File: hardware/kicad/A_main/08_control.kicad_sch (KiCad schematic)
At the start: 26 parts, among them J60 GPS modul, J61 SMA 10MHz ref, J62 DAC modul, J63 C kartina, J64 UART 3.3V, J65 C kartina #2, J66 D kartina, U10 LFE5U-25F-7BG256I, U62 TLV3501AIDBVR

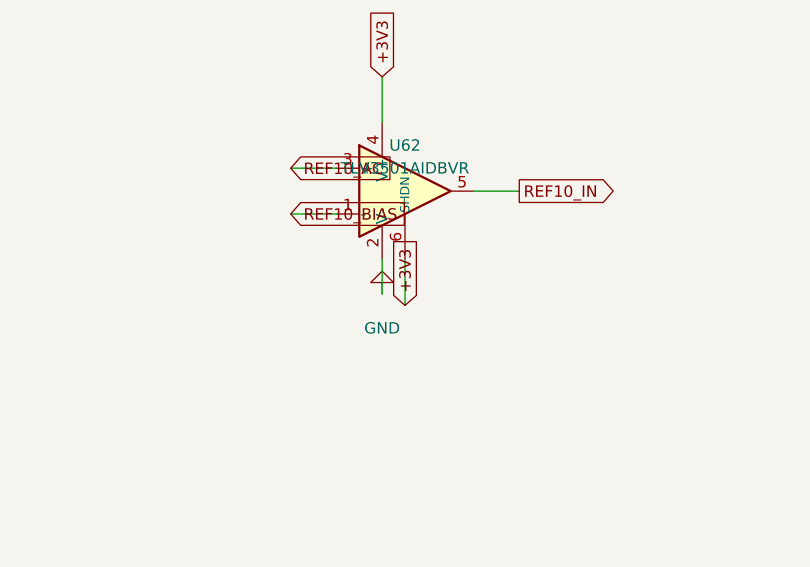
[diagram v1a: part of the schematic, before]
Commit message: Remove the pads that have no copper from the DSN export
The router reported the same 220 clearance violations in each pass.
At the same time the number of unrouted connections decreased. The
violations were thus in the input and not in the routing.

The -1EP footprints of KiCad put four paste apertures on the exposed
pad. These apertures stop full paste coverage and they have no copper
layer. The DSN export put them on the top copper layer. The image of
U51 in the DSN had 21 pins: 17 correct pins and four unconnected
copper islands in the exposed pad. These islands are always in
conflict with the pad and they close the area below it.

The export now removes a pad that has no copper layer. The image of
U51 has 17 pins. The violations on board D decreased from 220 to 152.
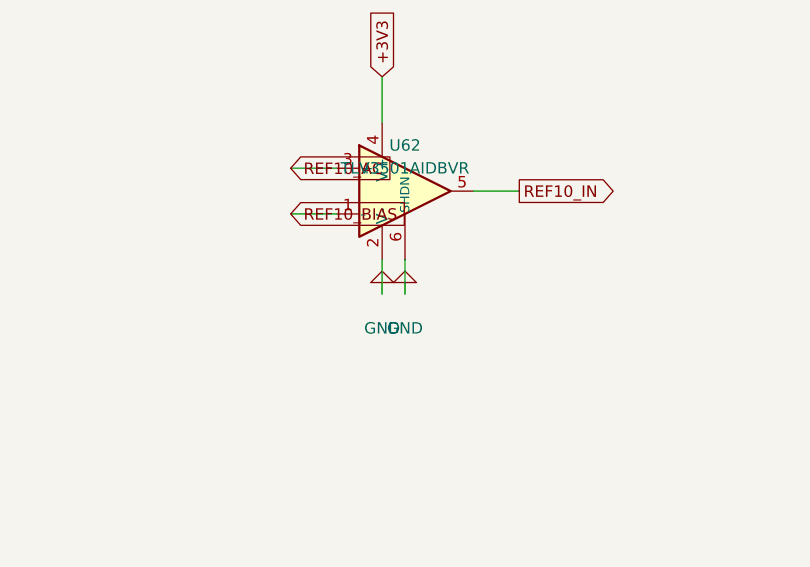
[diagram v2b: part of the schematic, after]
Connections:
- net +3V3: no longer U62.6 (SHDN)
- net GND: now also U62.6 (SHDN)

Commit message: Correct the clearance test for the pre-routed traces
The clearance test used a circle for each pad. The radius was
max(width, height)/2. The corner of a rectangle is at
hypot(width, height)/2 from the center. The test thus made the pad
smaller than it is. On the 2.5 x 4.5 mm gate pad of a TO-247 the
difference is 2.250 mm against 2.574 mm.

The DRN_A trace was on the gate pad of Q10 with an overlap of 35 um.
This is a short circuit between the 50 V drain rail and the gate of a
100 W device. The search that finds the tee offset accepted this
route. The overlap is at a corner and 35 um wide. You cannot see it
on a plot.

The test now uses the real shape of the pad and the collision test of
pcbnew. It also uses the 300 um clearance and not only an overlap. A
trace that is 50 um from a pad is also not possible to manufacture.

Board D was built again. No trace is below 300 um and the smallest
gap is 0.537 mm. Boards A and C were correct.
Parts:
- removed C900, C901, C902: 100nF, Capacitor_SMD:C_0603_1608Metric, symbol Device:C
- removed D60: yesil, LED_SMD:LED_0805_2012Metric, symbol Device:LED
- removed D61: mavi, LED_SMD:LED_0805_2012Metric, symbol Device:LED
- removed D62: kirmizi, LED_SMD:LED_0805_2012Metric, symbol Device:LED
- removed D63: sari, LED_SMD:LED_0805_2012Metric, symbol Device:LED
- removed J60: GPS modul, Connector_PinHeader_2.54mm:PinHeader_1x06_P2.54mm_Vertical, symbol Connector_Generic:Conn_01x06
- removed J61: SMA 10MHz ref, Connector_Coaxial:SMA_Amphenol_132289_EdgeMount, symbol Connector:Conn_Coaxial
- removed J62: DAC modul, Connector_PinHeader_2.54mm:PinHeader_1x06_P2.54mm_Vertical, symbol Connector_Generic:Conn_01x06
- removed J63: C kartina, Connector_PinHeader_2.54mm:PinHeader_2x10_P2.54mm_Vertical, symbol Connector_Generic:Conn_02x10_Odd_Even
- removed J64: UART 3.3V, Connector_PinHeader_2.54mm:PinHeader_1x04_P2.54mm_Vertical, symbol Connector_Generic:Conn_01x04
- removed J65: C kartina #2, Connector_PinHeader_2.54mm:PinHeader_1x06_P2.54mm_Vertical, symbol Connector_Generic:Conn_01x06
- removed J66: D kartina, Connector_PinHeader_2.54mm:PinHeader_2x10_P2.54mm_Vertical, symbol Connector_Generic:Conn_02x10_Odd_Even
- removed R60, R61, R62, R63: 1k, Resistor_SMD:R_0603_1608Metric, symbol Device:R
- removed R801: 0R, Resistor_SMD:R_0603_1608Metric, symbol Device:R
- removed R900: 50R 1%, Resistor_SMD:R_0603_1608Metric, symbol Device:R
- removed R901, R902, R903, R904: 10k, Resistor_SMD:R_0603_1608Metric, symbol Device:R
- removed U10: LFE5U-25F-7BG256I, Package_BGA:BGA-256_14.0x14.0mm_Layout16x16_P0.8mm_Ball0.45mm_Pad0.32mm_NSMD, symbol dogrudan-sdr:ECP5-BGA256
- removed U62: TLV3501AIDBVR, Package_TO_SOT_SMD:SOT-23-6, symbol Comparator:TLV3501AIDBV
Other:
- note added: "Kontrol PE4312 x2, GPS, VCXO DAC, roleler, banka 0/1 Baglantilar: ../NETLIST.md"
- note removed: "3.3 V TTL, CP2102/FT232 tarzi ucuz donusturucu takilir. Bringup'ta FPGA icindeki yazilim buradan konusuyor; JTAG'den once calisan tek gozlem yolu."
- note removed: "ANOT +3V3'te, FPGA KATODU CEKIYOR (aktif dusuk). Boyle secildi cunku ECP5'in IO'su akim CEKMEKTE (sink) akim VERMEKTEN (source) daha guclu: 3.3V bankada 8 mA sink, source tarafinda gerilim dusuyor ve LED sonuk kaliyor. 1k ile 3.3V'ta ~1.6 mA — 0805 LED icin fazlasiyla gorunur, dort LED toplam 6.4 mA. Parlaklik isterse 470R'a inilir. STATUS gateware kalkti / PLL kilitli RX alis zinciri veri uretiy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"
- note removed: "BANKA 0: 24 I/O, TAMAMI DOLU. SDRAM tasmasi 7 (A9-A12, BA0/1, UDQM) ADC SPI+SYNC 5 SDIO, SCLK, 2x nCSB, SYNC ortak seri yol 2 ATT_DATA, ATT_CLK secme hatlari 7 ATT1..4_LE, PA_ATT_LE, BIAS_CS1/CS2 PA'nin ADC'si 1 PA_ADC_CS role yazmaci 3 SER/SRCLK/RCLK ADC PDWN ve DAC SLEEP hatlari KALDIRILDI. Bu alet ya acik ya kapali; guc-dusurme kontrolu hic kullanilmiyor. Dordu de kendi sayfalarinda GND'ye bag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"
- note removed: "BANKA 1: 32/32, MARJ YOK. DAC-2 interleaved 17 · GPS 3 · VCXO DAC 3 · hata ayiklama UART 2 harici 10 MHz 1 · role RCLK 1 · T/R 4 · PA_INHIBIT 1 PA_INHIBIT yedek pini aldi. Donanim kesme hatti: FPGA sifirlaninca ya da beslemesizken D kartinda 100k asagi cekiyor ve surucu beslemesiz kaliyor. Bu hattin seri yola girmesi kabul edilemez — guvenlik dogrudan olmali. Durum LED'leri buraya sigmadi — 07_fp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"
- note removed: "D KARTINA (PA)"
- note removed: "DAC parcasi HENUZ SECILMEDI — 16 bit, dusuk gurultulu, SPI. Vc gurultusu dogrudan faz gurultusune donusuyor, o yuzden beslemesi +3V3_CLK (VCXO'nun kendi LDO'su). Baslik olarak cizildi; parca secilince yerine konacak."
- note removed: "DURUM LED'LERI"
- note removed: "FPGA BANKA 0 — kontrol ve SDRAM tasmasi"
- note removed: "FPGA BANKA 1 — GPSDO, DAC-2, durum"
- note removed: "GPS / GPSDO ARAYUZU"
- note removed: "HARICI 10 MHz — SMA, 50R sonlandirma, AC kuplaj, KOMPARATOR. Iki 10k bolucu orta gerilim (1.65 V) uretiyor: sinyal bacagi o gerilim etrafinda salınıyor, referans bacagi ayni gerilimde sabit (100nF ile susturulmus). Komparator birkac yuz mV'luk sinusu tam salinimli kare dalgaya ceviriyor. TLV3501AIDBVR, LCSC C193413, $1.57, 1850 stok, SOT-23-6. 4.5 ns gecikme, rail-to-rail giris, tek 3.3 V besleme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"
- note removed: "HATA AYIKLAMA UART"
- note removed: "HER SINYALIN YANINDA TOPRAK. 2.54 mm baslikta bitisik toprak donus yolunu kisaltiyor; role hatlari 12 V anahtarliyor ve kenarlari sert, yanindaki RF'e kuplaj yapmasin. ATT2 hatlari ve +12 V ikinci baslikta (yerlesimde eklenecek). RF kart arasi koaks kuyrukla — baslikla DEGIL. Toprak GND_HDR uzerinden 0R ile ana topraga: tek nokta, gerekirse ayrilabiliyor."
- note removed: "KART ARASI — A <-> C, NETLIST.md §8"
- note removed: "PA'nin istedigi 13 sinyal 5 YENI HATLA karsilandi: ATT_DATA / ATT_CLK -> C kartiyla ORTAK, yeni hat yok ADC_SDIO -> ortak MISO, AD9251'in hatti role zinciri -> D'ye C KARTINDAN gidiyor, A'dan degil PA_ATT_LE, BIAS_CS1, BIAS_CS2, PA_ADC_CS, PA_INHIBIT -> yeni FLANGE_T, FWD_LOG, REV_LOG analog olcumleri A kartina GELMIYOR: D kartinda bir MCP3208 (8 kanal 12 bit SPI ADC) var, ayni seri yolu paylasiy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"
- note removed: "PE4312 x2, 0-31.5 dB. Her birine uc hat: Data / Clock / LE. Seri mod (P/S = HIGH). Paralel modda alti adres bacagini surmek gerekirdi, iki cip icin 12 pin ederdi. ACILIS DURUMU C KARTINDA COZULUYOR: seri modda bile acilistaki zayiflatma C0.5..C16 bacaklarindaki seviyeye gore belirleniyor (veri sayfasi s.6). Altisi da 10k ile yukari -> 31.5 dB, yani acilista alici en sagir halinde. FPGA flash'tan 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"
- note removed: "VCXO Vc — SPI DAC"
- note removed: "ZAYIFLATICI KONTROLU — cipler C KARTINDA"

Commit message: Correct the schematic faults that ERC cannot find
An agent examined the three schematics against the datasheets. ERC
reported zero violations before and after this work. None of these
faults are visible to ERC.

The comparator for the external 10 MHz reference was in shutdown. The
SHDN pin of the TLV3501 went to +3V3. Sixteen DRV8833 devices had VCP
and VINT unconnected. Without the charge pump none of the 28 filter
relays can latch. Seven regulators had no decoupling capacitor within
18 mm to 94 mm. On board D the nearest +12V capacitor to an LM358 was
227 mm away on a 275 mm board.

The PE4312 devices had no series 10k resistor on pin 3. The datasheet
makes this necessary for the attenuation accuracy. Their exposed pad
was 2.6 mm against 2.15 mm. The BOM did not give the load capacitance
of the crystal. This work added 60 parts and changed 4 footprints.

The worst fault was in the tool chain. lib/gen_symbols.py still made
the old pin numbers. The five corrections went into the symbol
library by hand and not into its generator. A new library would have
removed all of them.

The thermal vias are now a decision from the measured clearance and
the dissipation. This work removed them from the PE4312, the RTL8211F
and the ADCLK846. They stay on the DRV8833 and on the LM5164, which
is a 1 W buck converter.

Two checks are new. sema_denetim compares the pin names with the
nets. netlist_denetim locks 22 pin-to-net expectations from the
datasheets and does not need a board.

The boards were built again with these corrections. The chain now
adds the test points: 10 on board A, 7 on board C and 15 on board D.
Each board has 3 fiducials. Every pad has a net.
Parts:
- added C900, C901, C902: 100nF, Capacitor_SMD:C_0603_1608Metric, symbol Device:C
- added D60: yesil, LED_SMD:LED_0805_2012Metric, symbol Device:LED
- added D61: mavi, LED_SMD:LED_0805_2012Metric, symbol Device:LED
- added D62: kirmizi, LED_SMD:LED_0805_2012Metric, symbol Device:LED
- added D63: sari, LED_SMD:LED_0805_2012Metric, symbol Device:LED
- added J60: GPS modul, Connector_PinHeader_2.54mm:PinHeader_1x06_P2.54mm_Vertical, symbol Connector_Generic:Conn_01x06
- added J61: SMA 10MHz ref, Connector_Coaxial:SMA_Amphenol_132289_EdgeMount, symbol Connector:Conn_Coaxial
- added J62: DAC modul, Connector_PinHeader_2.54mm:PinHeader_1x06_P2.54mm_Vertical, symbol Connector_Generic:Conn_01x06
- added J63: C kartina, Connector_PinHeader_2.54mm:PinHeader_2x10_P2.54mm_Vertical, symbol Connector_Generic:Conn_02x10_Odd_Even
- added J64: UART 3.3V, Connector_PinHeader_2.54mm:PinHeader_1x04_P2.54mm_Vertical, symbol Connector_Generic:Conn_01x04
- added J65: C kartina #2, Connector_PinHeader_2.54mm:PinHeader_1x06_P2.54mm_Vertical, symbol Connector_Generic:Conn_01x06
- added J66: D kartina, Connector_PinHeader_2.54mm:PinHeader_2x10_P2.54mm_Vertical, symbol Connector_Generic:Conn_02x10_Odd_Even
- added R60, R61, R62, R63: 1k, Resistor_SMD:R_0603_1608Metric, symbol Device:R
- added R801: 0R, Resistor_SMD:R_0603_1608Metric, symbol Device:R
- added R900: 50R 1%, Resistor_SMD:R_0603_1608Metric, symbol Device:R
- added R901, R902, R903, R904: 10k, Resistor_SMD:R_0603_1608Metric, symbol Device:R
- added U10: LFE5U-25F-7BG256I, Package_BGA:BGA-256_14.0x14.0mm_Layout16x16_P0.8mm_Ball0.45mm_Pad0.32mm_NSMD, symbol dogrudan-sdr:ECP5-BGA256
- added U62: TLV3501AIDBVR, Package_TO_SOT_SMD:SOT-23-6, symbol Comparator:TLV3501AIDBV
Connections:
- new net +3V3: C902.1, D60.2 (A), D61.2 (A), D62.2 (A), D63.2 (A), J60.1 (Pin_1), J63.1 (Pin_1), J64.1 (Pin_1), J65.5 (Pin_5), J66.1 (Pin_1), R901.1, R903.1, U10.F10 (VCCIO1_1), U10.F11 (VCCIO1_2), U10.F6 (VCCIO0_1), U10.F7 (VCCIO0_2), U62.4 (V+)
- new net +3V3_CLK: J62.1 (Pin_1)
- new net ADC1_nCSB: U10.B5 (PT15B)
- new net ADC2_nCSB: U10.B6 (PT22B)
- new net ADC_SCLK: U10.B4 (PT11B)
- new net ADC_SDIO: J66.17 (Pin_17), U10.B3 (PT4B)
- new net ADC_SYNC: U10.B7 (PT27B)
- new net ATT1_LE: J63.19 (Pin_19), U10.C6 (PT22A)
- new net ATT2_LE: J65.1 (Pin_1), U10.C7 (PT27A)
- new net ATT3_LE: J65.2 (Pin_2), U10.D4 (PT9B)
- new net ATT4_LE: J65.3 (Pin_3), U10.D5 (PT13B)
- new net ATT_CLK: J63.18 (Pin_18), J66.5 (Pin_5), U10.C5 (PT15A)
- new net ATT_DATA: J63.17 (Pin_17), J66.3 (Pin_3), U10.C4 (PT11A)
- new net BIAS_CS1: J66.9 (Pin_9), U10.D7 (PT24B)
- new net BIAS_CS2: J66.11 (Pin_11), U10.E4 (PT9A)
- new net DAC2_D0: U10.A9 (PT42A)
- new net DAC2_D1: U10.B9 (PT38A)
- new net DAC2_D10: U10.B13 (PT60A)
- new net DAC2_D11: U10.A14 (PT65B)
- new net DAC2_D12: U10.B14 (PT67A)
- new net DAC2_D13: U10.A15 (PT67B)
- new net DAC2_D2: U10.D9 (PT40A)
- new net DAC2_D3: U10.A10 (PT42B)
- new net DAC2_D4: U10.B10 (PT44A)
- new net DAC2_D5: U10.A11 (PT53A)
- new net DAC2_D6: U10.B11 (PT49A)
- new net DAC2_D7: U10.A12 (PT53B)
- new net DAC2_D8: U10.B12 (PT56A)
- new net DAC2_D9: U10.A13 (PT65A)
- new net DAC2_IQRESET: U10.C10 (PT44B)
- new net DAC2_IQSEL: U10.C11 (PT49B)
- new net DAC2_IQWRT: U10.B8 (PT35B)
- new net DBG_RX: J64.2 (Pin_2), U10.D12 (PT58A)
- new net DBG_TX: J64.3 (Pin_3), U10.D13 (PT62A)
- new net GND: C901.2, C902.2, J60.5 (Pin_5), J60.6 (Pin_6), J61.2 (Ext), J62.6 (Pin_6), J64.4 (Pin_4), J65.6 (Pin_6), R801.2, R900.2, R902.2, R904.2, U62.2 (V-), U62.6 (SHDN)
- new net GND_HDR: J63.10 (Pin_10), J63.12 (Pin_12), J63.14 (Pin_14), J63.16 (Pin_16), J63.2 (Pin_2), J63.4 (Pin_4), J63.6 (Pin_6), J63.8 (Pin_8), J66.10 (Pin_10), J66.12 (Pin_12), J66.14 (Pin_14), J66.16 (Pin_16), J66.18 (Pin_18), J66.19 (Pin_19), J66.2 (Pin_2), J66.20 (Pin_20), J66.4 (Pin_4), J66.6 (Pin_6), J66.8 (Pin_8), R801.1
- new net GPS_1PPS: J60.4 (Pin_4), U10.C12 (PT56B)
- new net GPS_RX: J60.2 (Pin_2), U10.C13 (PT60B)
- new net GPS_TX: J60.3 (Pin_3), U10.C8 (PT35A)
- new net LED_DATA: R63.2
- new net LED_DATA_K: D63.1 (K), R63.1
- new net LED_RX: R61.2
- new net LED_RX_K: D61.1 (K), R61.1
- new net LED_STATUS: R60.2
- new net LED_STATUS_K: D60.1 (K), R60.1
- new net LED_TX: R62.2
- new net LED_TX_K: D62.1 (K), R62.1
- new net PA_ADC_CS: J66.13 (Pin_13), U10.E5 (PT13A)
- new net PA_ATT_LE: J66.7 (Pin_7), U10.D6 (PT20B)
- new net PA_INHIBIT: J66.15 (Pin_15), U10.E9 (PT40B)
- new net REF10_AC: C900.2, R901.2, R902.1, U62.3 (+)
- new net REF10_BIAS: C901.1, R903.2, R904.1, U62.1 (-)
- new net REF10_IN: U10.D8 (PT33B), U62.5
- new net REF10_RAW: C900.1, J61.1 (In), R900.1
- new net RLY_RCLK: J63.7 (Pin_7), U10.E10 (PT47B)
- new net RLY_SER: J63.3 (Pin_3), U10.E6 (PT20A)
- new net RLY_SRCLK: J63.5 (Pin_5), U10.E7 (PT24A)
- new net SD_A10: U10.A2 (PT4A)
- new net SD_A11: U10.A6 (PT18B)
- new net SD_A12: U10.A7 (PT29A)
- new net SD_A9: U10.A5 (PT18A)
- new net SD_BA0: U10.A3 (PT6A)
- new net SD_BA1: U10.A4 (PT6B)
- new net SD_UDQM: U10.A8 (PT29B)
- new net TR1: J63.9 (Pin_9), U10.E11 (PT51B)
- new net TR2: J63.11 (Pin_11), U10.E12 (PT58B)
- new net TR3: J63.13 (Pin_13), U10.E13 (PT62B)
- new net TR4: J63.15 (Pin_15), U10.E8 (PT33A)
- new net VCXO_CLK: J62.3 (Pin_3), U10.D10 (PT47A)
- new net VCXO_CS: J62.2 (Pin_2), U10.C9 (PT38B)
- new net VCXO_DIN: J62.4 (Pin_4), U10.D11 (PT51A)
- new net VCXO_VC: J62.5 (Pin_5)
- new net VIN_PROT: J63.20 (Pin_20), J65.4 (Pin_4)
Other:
- note added: "3.3 V TTL, CP2102/FT232 tarzi ucuz donusturucu takilir. Bringup'ta FPGA icindeki yazilim buradan konusuyor; JTAG'den once calisan tek gozlem yolu."
- note added: "ANOT +3V3'te, FPGA KATODU CEKIYOR (aktif dusuk). Boyle secildi cunku ECP5'in IO'su akim CEKMEKTE (sink) akim VERMEKTEN (source) daha guclu: 3.3V bankada 8 mA sink, source tarafinda gerilim dusuyor ve LED sonuk kaliyor. 1k ile 3.3V'ta ~1.6 mA — 0805 LED icin fazlasiyla gorunur, dort LED toplam 6.4 mA. Parlaklik isterse 470R'a inilir. STATUS gateware kalkti / PLL kilitli RX alis zinciri veri uretiy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"
- note added: "BANKA 0: 24 I/O, TAMAMI DOLU. SDRAM tasmasi 7 (A9-A12, BA0/1, UDQM) ADC SPI+SYNC 5 SDIO, SCLK, 2x nCSB, SYNC ortak seri yol 2 ATT_DATA, ATT_CLK secme hatlari 7 ATT1..4_LE, PA_ATT_LE, BIAS_CS1/CS2 PA'nin ADC'si 1 PA_ADC_CS role yazmaci 3 SER/SRCLK/RCLK ADC PDWN ve DAC SLEEP hatlari KALDIRILDI. Bu alet ya acik ya kapali; guc-dusurme kontrolu hic kullanilmiyor. Dordu de kendi sayfalarinda GND'ye bag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"
- note added: "BANKA 1: 32/32, MARJ YOK. DAC-2 interleaved 17 · GPS 3 · VCXO DAC 3 · hata ayiklama UART 2 harici 10 MHz 1 · role RCLK 1 · T/R 4 · PA_INHIBIT 1 PA_INHIBIT yedek pini aldi. Donanim kesme hatti: FPGA sifirlaninca ya da beslemesizken D kartinda 100k asagi cekiyor ve surucu beslemesiz kaliyor. Bu hattin seri yola girmesi kabul edilemez — guvenlik dogrudan olmali. Durum LED'leri buraya sigmadi — 07_fp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"
- note added: "D KARTINA (PA)"
- note added: "DAC parcasi HENUZ SECILMEDI — 16 bit, dusuk gurultulu, SPI. Vc gurultusu dogrudan faz gurultusune donusuyor, o yuzden beslemesi +3V3_CLK (VCXO'nun kendi LDO'su). Baslik olarak cizildi; parca secilince yerine konacak."
- note added: "DURUM LED'LERI"
- note added: "FPGA BANKA 0 — kontrol ve SDRAM tasmasi"
- note added: "FPGA BANKA 1 — GPSDO, DAC-2, durum"
- note added: "GPS / GPSDO ARAYUZU"
- note added: "HARICI 10 MHz — SMA, 50R sonlandirma, AC kuplaj, KOMPARATOR. Iki 10k bolucu orta gerilim (1.65 V) uretiyor: sinyal bacagi o gerilim etrafinda salınıyor, referans bacagi ayni gerilimde sabit (100nF ile susturulmus). Komparator birkac yuz mV'luk sinusu tam salinimli kare dalgaya ceviriyor. TLV3501AIDBVR, LCSC C193413, $1.57, 1850 stok, SOT-23-6. 4.5 ns gecikme, rail-to-rail giris, tek 3.3 V besleme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"
- note added: "HATA AYIKLAMA UART"
- note added: "HER SINYALIN YANINDA TOPRAK. 2.54 mm baslikta bitisik toprak donus yolunu kisaltiyor; role hatlari 12 V anahtarliyor ve kenarlari sert, yanindaki RF'e kuplaj yapmasin. ATT2 hatlari ve +12 V ikinci baslikta (yerlesimde eklenecek). RF kart arasi koaks kuyrukla — baslikla DEGIL. Toprak GND_HDR uzerinden 0R ile ana topraga: tek nokta, gerekirse ayrilabiliyor."
- note added: "KART ARASI — A <-> C, NETLIST.md §8"
- note added: "PA'nin istedigi 13 sinyal 5 YENI HATLA karsilandi: ATT_DATA / ATT_CLK -> C kartiyla ORTAK, yeni hat yok ADC_SDIO -> ortak MISO, AD9251'in hatti role zinciri -> D'ye C KARTINDAN gidiyor, A'dan degil PA_ATT_LE, BIAS_CS1, BIAS_CS2, PA_ADC_CS, PA_INHIBIT -> yeni FLANGE_T, FWD_LOG, REV_LOG analog olcumleri A kartina GELMIYOR: D kartinda bir MCP3208 (8 kanal 12 bit SPI ADC) var, ayni seri yolu paylasiy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"
- note added: "PE4312 x2, 0-31.5 dB. Her birine uc hat: Data / Clock / LE. Seri mod (P/S = HIGH). Paralel modda alti adres bacagini surmek gerekirdi, iki cip icin 12 pin ederdi. ACILIS DURUMU C KARTINDA COZULUYOR: seri modda bile acilistaki zayiflatma C0.5..C16 bacaklarindaki seviyeye gore belirleniyor (veri sayfasi s.6). Altisi da 10k ile yukari -> 31.5 dB, yani acilista alici en sagir halinde. FPGA flash'tan 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"
- note added: "VCXO Vc — SPI DAC"
- note added: "ZAYIFLATICI KONTROLU — cipler C KARTINDA"
- note removed: "Kontrol PE4312 x2, GPS, VCXO DAC, roleler, banka 0/1 Baglantilar: ../NETLIST.md"
